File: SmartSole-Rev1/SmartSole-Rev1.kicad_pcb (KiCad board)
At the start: 2 copper layers, 37.4 x 68.6 mm, 22 parts, among them J1 5103310-5, J2 1-825433-2, J3 1-825433-2, U1 MCP6004, U2 MCP6004, U3 AD1583

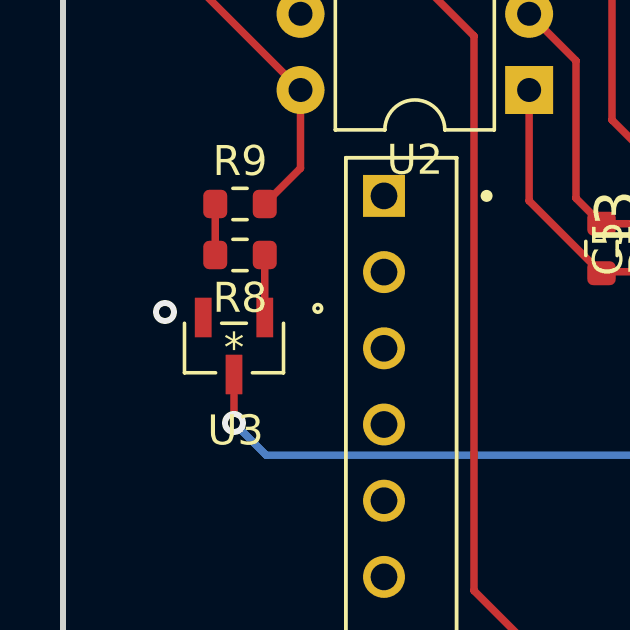
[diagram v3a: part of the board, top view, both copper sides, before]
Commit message: First review with rachel, made notes on changes to be made
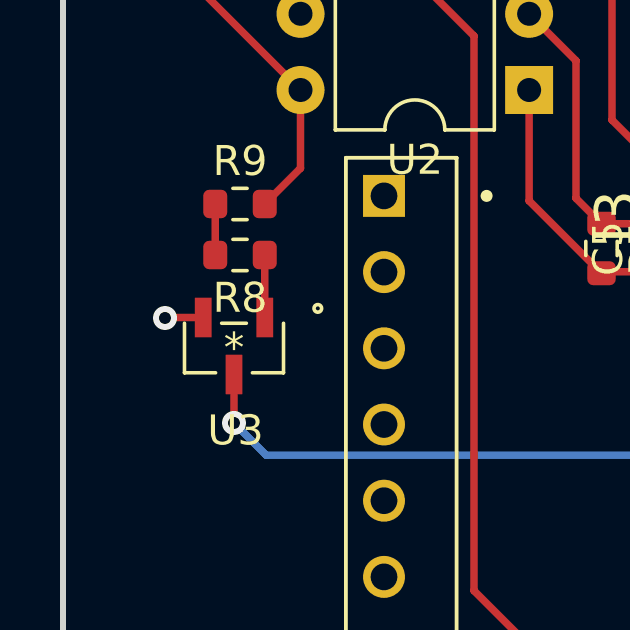
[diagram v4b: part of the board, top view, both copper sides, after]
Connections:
- U1 pad 11: unconnected-(U1-Pad11) -> GND
- U2 pad 11: unconnected-(U2-Pad11) -> GND
- U2 pad 4: unconnected-(U2-Pad4) -> /3.3V
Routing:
- net GND: track 0.00 -> 1.28 mm
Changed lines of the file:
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@@
   (net 9 "GND")
   (net 10 "/AIN5")
-  (net 11 "unconnected-(U1-Pad11)")
+  (net 11 "Net-(R8-Pad2)")
   (net 12 "/ForceIn_4")
   (net 13 "/AIN1")
@@
   (net 38 "unconnected-(J3-Pad12)")
   (net 39 "Net-(R8-Pad1)")
-  (net 40 "Net-(R9-Pad1)")
-  (net 41 "unconnected-(U2-Pad4)")
-  (net 42 "unconnected-(U2-Pad11)")
   (footprint "CapstoneLibrary:TE_1-825433-2" locked (layer "F.Cu")
     (at 127 114.3 -90)
@@
     (fp_circle (center -13.97 -3.42) (end -13.87 -3.42) (layer "F.Fab") (width 0.2) (fill none))
     (pad "1" thru_hole rect locked (at -13.97 0 270) (size 1.398 1.398) (drill 0.89) (layers *.Cu *.Mask)
-      (net 27 "unconnected-(J3-Pad1)") (pinfunction "1") (pintype "passive"))
+      (net 27 "unconnected-(J3-Pad1)") (pinfunction "1") (pintype "passive+no_connect"))
     (pad "2" thru_hole circle locked (at -11.43 0 270) (size 1.398 1.398) (drill 0.89) (layers *.Cu *.Mask)
-      (net 28 "unconnected-(J3-Pad2)") (pinfunction "2") (pintype "passive"))
+      (net 28 "unconnected-(J3-Pad2)") (pinfunction "2") (pintype "passive+no_connect"))
     (pad "3" thru_hole circle locked (at -8.89 0 270) (size 1.398 1.398) (drill 0.89) (layers *.Cu *.Mask)
-      (net 29 "unconnected-(J3-Pad3)") (pinfunction "3") (pintype "passive"))
+      (net 29 "unconnected-(J3-Pad3)") (pinfunction "3") (pintype "passive+no_connect"))
     (pad "4" thru_hole circle locked (at -6.35 0 270) (size 1.398 1.398) (drill 0.89) (layers *.Cu *.Mask)
-      (net 30 "unconnected-(J3-Pad4)") (pinfunction "4") (pintype "passive"))
+      (net 30 "unconnected-(J3-Pad4)") (pinfunction "4") (pintype "passive+no_connect"))
     (pad "5" thru_hole circle locked (at -3.81 0 270) (size 1.398 1.398) (drill 0.89) (layers *.Cu *.Mask)
-      (net 31 "unconnected-(J3-Pad5)") (pinfunction "5") (pintype "passive"))
+      (net 31 "unconnected-(J3-Pad5)") (pinfunction "5") (pintype "passive+no_connect"))
     (pad "6" thru_hole circle locked (at -1.27 0 270) (size 1.398 1.398) (drill 0.89) (layers *.Cu *.Mask)
-      (net 32 "unconnected-(J3-Pad6)") (pinfunction "6") (pintype "passive"))
+      (net 32 "unconnected-(J3-Pad6)") (pinfunction "6") (pintype "passive+no_connect"))
     (pad "7" thru_hole circle locked (at 1.27 0 270) (size 1.398 1.398) (drill 0.89) (layers *.Cu *.Mask)
-      (net 33 "unconnected-(J3-Pad7)") (pinfunction "7") (pintype "passive"))
+      (net 33 "unconnected-(J3-Pad7)") (pinfunction "7") (pintype "passive+no_connect"))
     (pad "8" thru_hole circle locked (at 3.81 0 270) (size 1.398 1.398) (drill 0.89) (layers *.Cu *.Mask)
-      (net 34 "unconnected-(J3-Pad8)") (pinfunction "8") (pintype "passive"))
+      (net 34 "unconnected-(J3-Pad8)") (pinfunction "8") (pintype "passive+no_connect"))
     (pad "9" thru_hole circle locked (at 6.35 0 270) (size 1.398 1.398) (drill 0.89) (layers *.Cu *.Mask)
-      (net 35 "unconnected-(J3-Pad9)") (pinfunction "9") (pintype "passive"))
+      (net 35 "unconnected-(J3-Pad9)") (pinfunction "9") (pintype "passive+no_connect"))
     (pad "10" thru_hole circle locked (at 8.89 0 270) (size 1.398 1.398) (drill 0.89) (layers *.Cu *.Mask)
-      (net 36 "unconnected-(J3-Pad10)") (pinfunction "10") (pintype "passive"))
+      (net 36 "unconnected-(J3-Pad10)") (pinfunction "10") (pintype "passive+no_connect"))
     (pad "11" thru_hole circle locked (at 11.43 0 270) (size 1.398 1.398) (drill 0.89) (layers *.Cu *.Mask)
-      (net 37 "unconnected-(J3-Pad11)") (pinfunction "11") (pintype "passive"))
+      (net 37 "unconnected-(J3-Pad11)") (pinfunction "11") (pintype "passive+no_connect"))
     (pad "12" thru_hole circle locked (at 13.97 0 270) (size 1.398 1.398) (drill 0.89) (layers *.Cu *.Mask)
-      (net 38 "unconnected-(J3-Pad12)") (pinfunction "12") (pintype "passive"))
+      (net 38 "unconnected-(J3-Pad12)") (pinfunction "12") (pintype "passive+no_connect"))
     (model "C:/Users/julia/Downloads/1-825433-2/1-825433-2.step"
       (offset (xyz 0 0 2.9))
@@
     (fp_line (start 0.8 0.4125) (end -0.8 0.4125) (layer "F.Fab") (width 0.1))
     (pad "1" smd roundrect locked (at -0.825 0) (size 0.8 0.95) (layers "F.Cu" "F.Paste" "F.Mask") (roundrect_rratio 0.25)
-      (net 40 "Net-(R9-Pad1)") (pintype "passive"))
+      (net 11 "Net-(R8-Pad2)") (pintype "passive"))
     (pad "2" smd roundrect locked (at 0.825 0) (size 0.8 0.95) (layers "F.Cu" "F.Paste" "F.Mask") (roundrect_rratio 0.25)
       (net 17 "/VRef") (pintype "passive"))
@@
       (net 39 "Net-(R8-Pad1)") (pintype "passive"))
     (pad "2" smd roundrect locked (at 0.825 0 180) (size 0.8 0.95) (layers "F.Cu" "F.Paste" "F.Mask") (roundrect_rratio 0.25)
-      (net 40 "Net-(R9-Pad1)") (pintype "passive"))
+      (net 11 "Net-(R8-Pad2)") (pintype "passive"))
     (model "${KICAD6_3DMODEL_DIR}/Resistor_SMD.3dshapes/R_0603_1608Metric.wrl"
       (offset (xyz 0 0 0))
@@
       (net 9 "GND") (pinfunction "+") (pintype "input"))
     (pad "4" thru_hole oval locked (at 0 7.62 180) (size 1.6 1.6) (drill 0.8) (layers *.Cu *.Mask)
-      (net 41 "unconnected-(U2-Pad4)") (pinfunction "V+") (pintype "power_in"))
+      (net 25 "/3.3V") (pinfunction "V+") (pintype "power_in"))
     (pad "5" thru_hole oval locked (at 0 10.16 180) (size 1.6 1.6) (drill 0.8) (layers *.Cu *.Mask)
       (net 9 "GND") (pinfunction "+") (pintype "input"))
@@
       (net 9 "GND") (pinfunction "+") (pintype "input"))
     (pad "11" thru_hole oval locked (at 7.62 7.62 180) (size 1.6 1.6) (drill 0.8) (layers *.Cu *.Mask)
-      (net 42 "unconnected-(U2-Pad11)") (pinfunction "V-") (pintype "power_in"))
+      (net 9 "GND") (pinfunction "V-") (pintype "power_in"))
     (pad "12" thru_hole oval locked (at 7.62 5.08 180) (size 1.6 1.6) (drill 0.8) (layers *.Cu *.Mask)
       (net 9 "GND") (pinfunction "+") (pintype "input"))
     (pad "13" thru_hole oval locked (at 7.62 2.54 180) (size 1.6 1.6) (drill 0.8) (layers *.Cu *.Mask)
-      (net 40 "Net-(R9-Pad1)") (pinfunction "-") (pintype "input"))
+      (net 11 "Net-(R8-Pad2)") (pinfunction "-") (pintype "input"))
     (pad "14" thru_hole oval locked (at 7.62 0 180) (size 1.6 1.6) (drill 0.8) (layers *.Cu *.Mask)
       (net 17 "/VRef") (pintype "output"))
@@
       (net 9 "GND") (pinfunction "+") (pintype "input"))
     (pad "11" thru_hole oval locked (at 7.62 7.62 180) (size 1.6 1.6) (drill 0.8) (layers *.Cu *.Mask)
-      (net 11 "unconnected-(U1-Pad11)") (pinfunction "V-") (pintype "power_in"))
+      (net 9 "GND") (pinfunction "V-") (pintype "power_in"))
     (pad "12" thru_hole oval locked (at 7.62 5.08 180) (size 1.6 1.6) (drill 0.8) (layers *.Cu *.Mask)
       (net 9 "GND") (pinfunction "+") (pintype "input"))
@@
     (pts (xy 116.299999 63.4) (xy 116.299999 131.98))
     (height 3.899999)
-    (gr_text "2700.0000 mils" (at 110.6 97.69 90) (layer "B.Cu")
+    (gr_text "2.7000 in" (at 110.6 97.69 90) (layer "B.Cu")
       (effects (font (size 1.5 1.5) (thickness 0.3)))
     )
@@
     (pts (xy 115.8 63.4) (xy 153.9 63.4))
     (height -7)
-    (gr_text "1500.0000 mils" (at 134.85 54.6) (layer "Cmts.User")
+    (gr_text "1.5000 in" (at 134.85 54.6) (layer "Cmts.User")
       (effects (font (size 1.5 1.5) (thickness 0.3)))
     )
@@
   (segment (start 131.8375 94.26) (end 133.4 95.8225) (width 0.25) (layer "F.Cu") (net 8))
   (segment (start 133.4 95.8225) (end 133.4 100.407602) (width 0.25) (layer "F.Cu") (net 8))
-  (via (at 119.699989 104.199995) (size 0.8) (drill 0.4) (layers "F.Cu" "B.Cu") (free) (net 9))
+  (segment (start 119.699989 104.4) (end 119.715987 104.384002) (width 0.25) (layer "F.Cu") (net 9))
+  (segment (start 119.715987 104.384002) (end 120.975008 104.384002) (width 0.25) (layer "F.Cu") (net 9))
+  (via (at 119.699989 104.4) (size 0.8) (drill 0.4) (layers "F.Cu" "B.Cu") (free) (net 9))
   (segment (start 138.525 96.725) (end 138.1298 96.3298) (width 0.25) (layer "F.Cu") (net 10))
   (segment (start 139.4575 96.725) (end 138.525 96.725) (width 0.25) (layer "F.Cu") (net 10))
@@
   (segment (start 137.4402 96.3798) (end 137.4902 96.3298) (width 0.25) (layer "F.Cu") (net 10))
   (segment (start 135.8392 96.3798) (end 137.4402 96.3798) (width 0.25) (layer "F.Cu") (net 10))
+  (segment (start 121.375 102.3) (end 121.375 100.6) (width 0.25) (layer "F.Cu") (net 11))
   (segment (start 134.25048 83.25048) (end 134.25048 79.93048) (width 0.25) (layer "F.Cu") (net 12))
   (segment (start 137.5 94.77) (end 137.4902 94.7798) (width 0.25) (layer "F.Cu") (net 12))
@@
   (segment (start 123.025 102.3) (end 123.025006 102.300006) (width 0.25) (layer "F.Cu") (net 39))
   (segment (start 122.85 102.3) (end 123.025 102.3) (width 0.25) (layer "F.Cu") (net 39))
-  (segment (start 121.375 102.3) (end 121.375 100.6) (width 0.25) (layer "F.Cu") (net 40))
 )

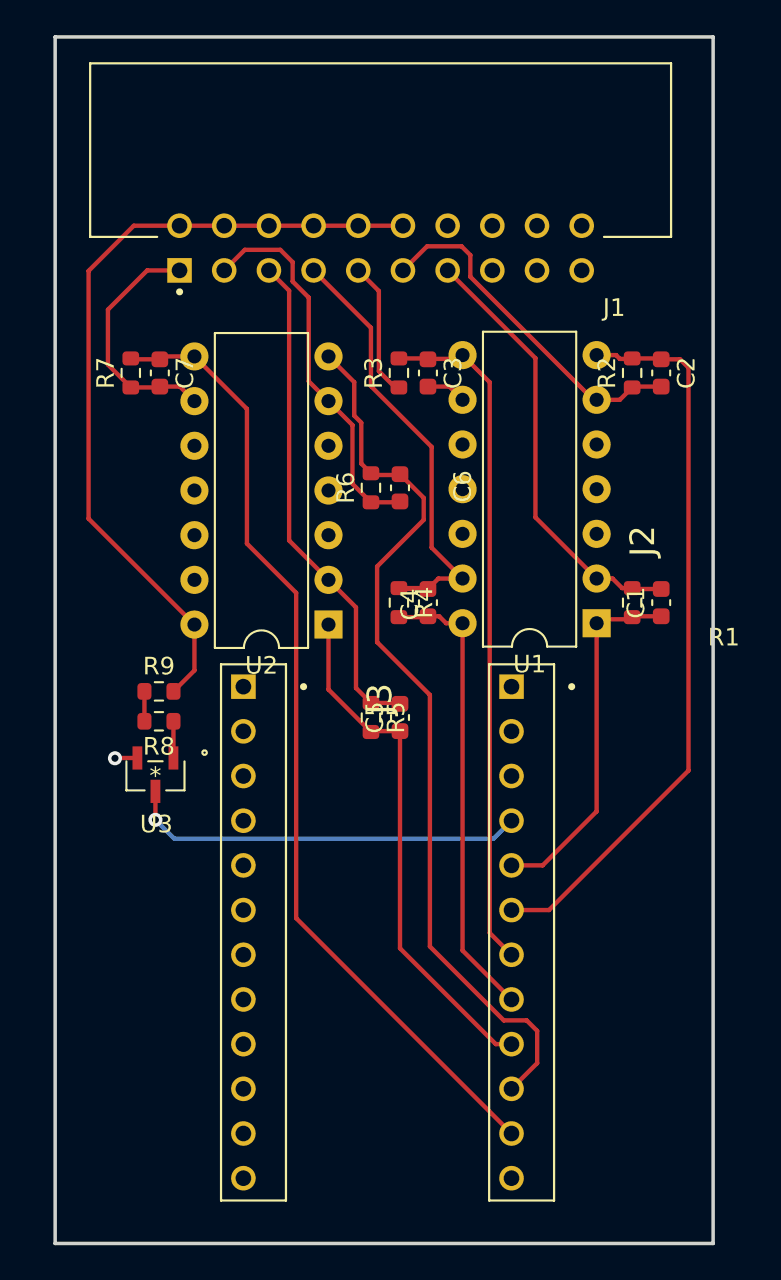
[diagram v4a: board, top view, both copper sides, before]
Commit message: Completed updates for schematic and PCB as noted from last review with rachel, DRC only warnings
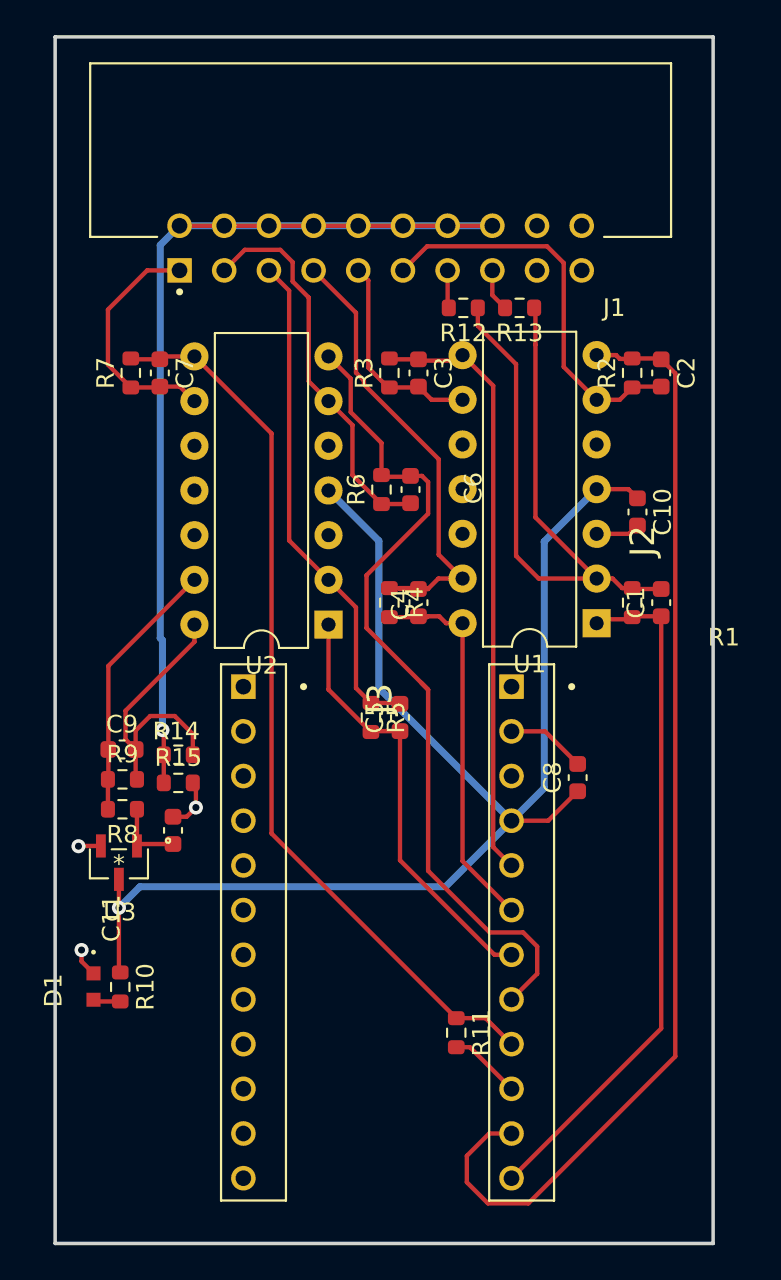
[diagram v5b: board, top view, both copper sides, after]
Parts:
- added C10: 4.7u, Capacitor_SMD:C_0603_1608Metric, F.Cu at (149.4, 90.4)
- added C11: 1u, Capacitor_SMD:C_0603_1608Metric, F.Cu at (123.0, 108.5)
- added C8: 0.1u, Capacitor_SMD:C_0603_1608Metric, F.Cu at (146.0, 105.5)
- added C9: .01u, Capacitor_SMD:C_0603_1608Metric, F.Cu at (120.1, 103.9)
- added D1: VLMG1300-GS08, CapstoneLibrary:VLMG1300-GS08, F.Cu at (118.5, 117.4)
- added R10: 10k, Resistor_SMD:R_0603_1608Metric, F.Cu at (120.0, 117.4)
- added R11: 0 - DNP, Resistor_SMD:R_0603_1608Metric, F.Cu at (139.1, 120.0)
- added R12: 0, Resistor_SMD:R_0603_1608Metric, F.Cu at (139.5, 78.8)
- added R13: 0 - DNP, Resistor_SMD:R_0603_1608Metric, F.Cu at (142.7, 78.8)
- added R14: 0, Resistor_SMD:R_0603_1608Metric, F.Cu at (123.3, 104.2)
- added R15: 0 - DNP, Resistor_SMD:R_0603_1608Metric, F.Cu at (123.3, 105.8)
- R8, R9: value R -> 680
- moved R8 5.41 mm to (120.1, 107.3)
- moved R9 5.41 mm to (120.1, 105.6)
- moved U3 5.41 mm to (119.9, 110.4)
- moved C6 0.61 mm to (136.5, 89.1)
- moved R6 0.61 mm to (134.8, 89.1)
- moved C3 0.54 mm to (137.0, 82.5)
- moved R3 0.54 mm to (135.3, 82.5)
- moved C4 0.54 mm to (137.0, 95.6)
- moved R4 0.54 mm to (135.3, 95.6)
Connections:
- C1 pad 1: /AIN2 -> /AIN0
- C1 pad 2: /ForceIn_1 -> /ForceIn_0
- C2 pad 1: /AIN3 -> /AIN1
- C3 pad 1: /AIN4 -> /AIN2
- C4 pad 1: /AIN5 -> /AIN3
- C5 pad 1: /AIN6 -> /AIN4
- C6 pad 1: /AIN7 -> /AIN5
- C7 pad 1: /AIN1 -> /AIN6
- J1 pad 13: /ForceIn_1 -> Net-(J1-Pad13)
- J1 pad 15: unconnected-(J1-Pad15) -> Net-(J1-Pad15)
- J2 pad 10: /AIN7 -> Net-(J2-Pad10)
- R1 pad 1: /ForceIn_1 -> /ForceIn_0
- R1 pad 2: /AIN2 -> /AIN0
- R2 pad 2: /AIN3 -> /AIN1
- R3 pad 2: /AIN4 -> /AIN2
- R4 pad 2: /AIN5 -> /AIN3
- R5 pad 2: /AIN6 -> /AIN4
- R6 pad 2: /AIN7 -> /AIN5
- R7 pad 2: /AIN1 -> /AIN6
- R9 pad 2: /VRef -> Net-(R9-Pad2)
- U1 pad 1: /AIN2 -> /AIN0
- U1 pad 14: /AIN5 -> /AIN3
- U1 pad 2: /ForceIn_1 -> /ForceIn_0
- U1 pad 7: /AIN3 -> /AIN1
- U1 pad 8: /AIN4 -> /AIN2
- U2 pad 1: /AIN6 -> /AIN4
- U2 pad 14: /VRef -> Net-(R9-Pad2)
- U2 pad 7: /AIN7 -> /AIN5
- U2 pad 8: /AIN1 -> /AIN6
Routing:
- net /3.3V: track 22.7 -> 80.6 mm
- net /AIN7: track 51.0 -> 0.00 mm
- net /ForceIn_0: track 0.00 -> 40.9 mm
- net /AIN0: track 0.00 -> 39.3 mm
- net /ForceIn_1: track 24.9 -> 0.00 mm
- net /VRef: track 45.8 -> 67.8 mm, vias 0 -> 1
- net /AIN6: track 29.7 -> 51.2 mm
- net /AIN5: track 26.9 -> 48.0 mm
- net /AIN3: track 41.8 -> 21.8 mm
- net Net-(R9-Pad2): track 0.00 -> 17.1 mm
- net /AIN4: track 39.0 -> 24.7 mm
- net /AIN2: track 20.6 -> 34.8 mm
- net Net-(R8-Pad2): track 1.70 -> 15.1 mm
- net GND: track 1.28 -> 12.9 mm, vias 1 -> 3
- net /AIN1: track 55.3 -> 64.1 mm
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- added copper zone on B.Cu, net GND
